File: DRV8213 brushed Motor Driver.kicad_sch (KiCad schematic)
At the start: 26 parts, among them J1 Keystone 3569, J10 1.27mm pin header, J11 1.27mm pin header, J2 Keystone 3579, J3 Keystone 3579, J4 Keystone 3569, J5 Keystone 3569, J6 Keystone 3579, J7 Keystone 3579, J8 Keystone 3569, J9 JST PH 2mm horizontal, U1 DRV8213RTER, U2 LP2981-3.3

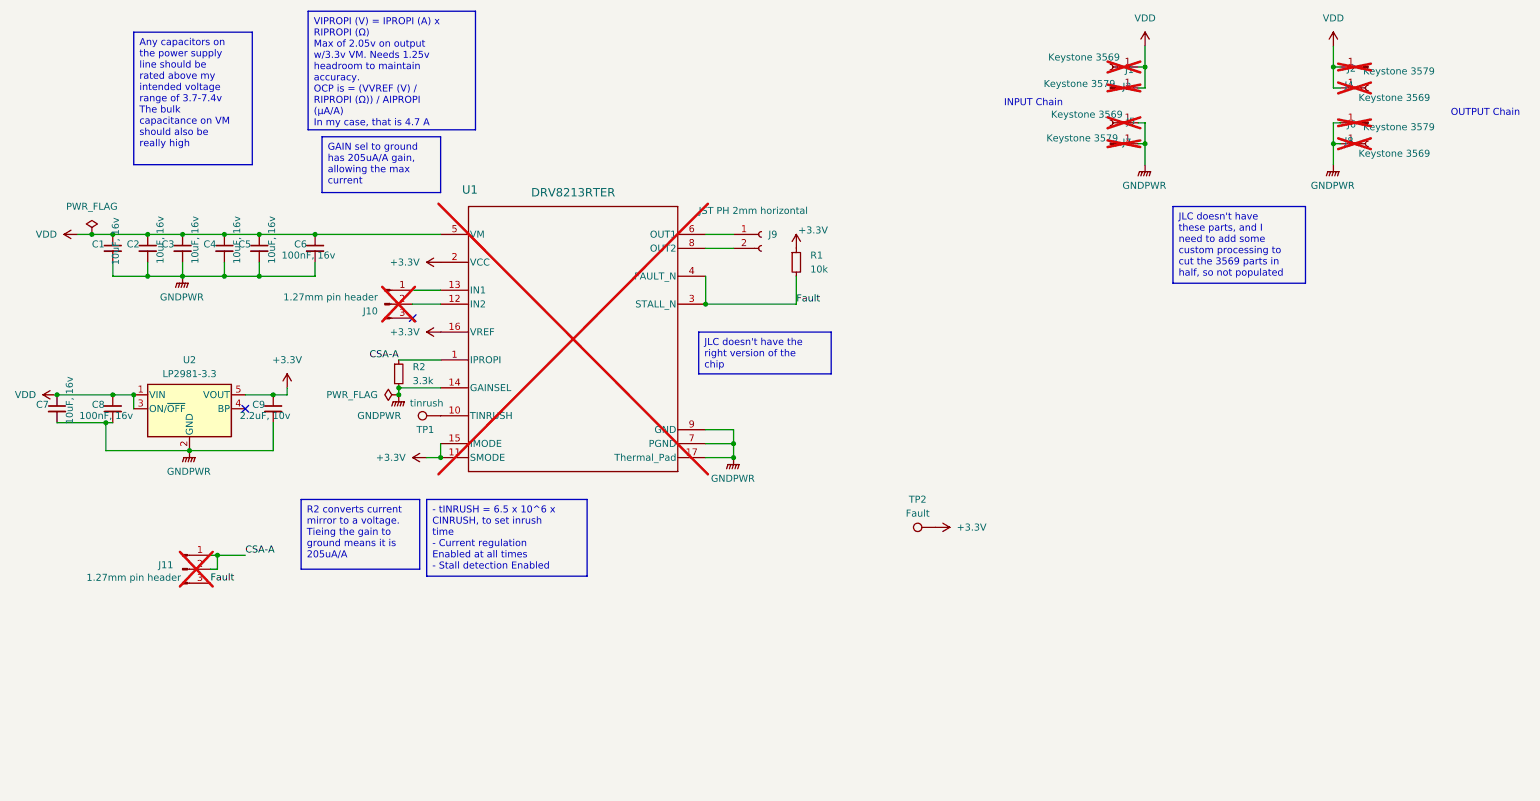
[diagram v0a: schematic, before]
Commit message: Updated connector parts in schematic
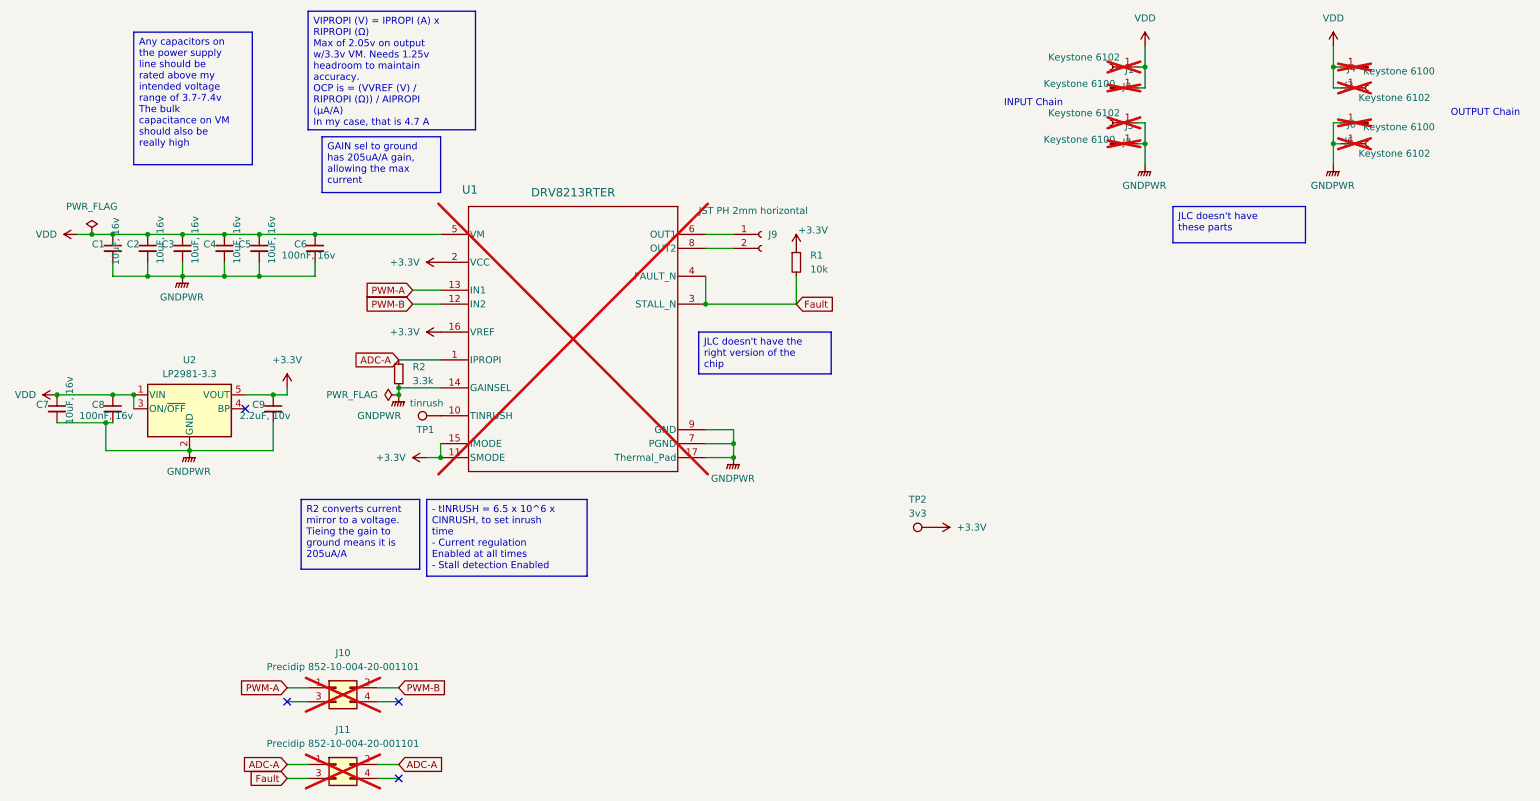
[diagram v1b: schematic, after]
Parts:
- removed J10, J11: 1.27mm pin header, Connector_PinHeader_1.27mm:PinHeader_1x03_P1.27mm_Horizontal, symbol Connector:Conn_01x03_Pin
- removed J2, J6: Keystone 3579, custom_Connector:Keystone_3579, symbol Connector:Conn_01x01_Pin
- removed J4, J8: Keystone 3569, custom_Connector:Keystone_3569_half, symbol Connector:Conn_01x01_Socket
- added J10, J11: Precidip 852-10-004-20-001101, custom_Connector:Precidip 852-10-004-20-001101, symbol Connector_Generic:Conn_02x02_Odd_Even
- added J2, J6: Keystone 6102, custom_Connector:Keystone_6102, symbol Connector:Conn_01x01_Socket
- added J4, J8: Keystone 6100, custom_Connector:Keystone_6100, symbol Connector:Conn_01x01_Pin
- J1, J5: value Keystone 3569 -> Keystone 6102; footprint custom_Connector:Keystone_3569_half -> custom_Connector:Keystone_6102
- J3, J7: value Keystone 3579 -> Keystone 6100; footprint custom_Connector:Keystone_3579 -> custom_Connector:Keystone_6100
- TP2: value Fault -> 3v3
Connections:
- net Fault: now also J11.3 (Pin_3)
- net GNDPWR: now also J6.1 (Pin_1), J8.1 (Pin_1)
- net VDD: now also J2.1 (Pin_1), J4.1 (Pin_1)
- net PWM-B: now reaches U1.12 (IN2)
- net PWM-B: now also J10.2 (Pin_2)
- net PWM-A: now reaches U1.13 (IN1)
- net PWM-A: now also J10.1 (Pin_1)
- net CSA-A renamed ADC-A
- net ADC-A: now also J11.1 (Pin_1), J11.2 (Pin_2)
- no-connect marks 2 -> 4
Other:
- title: (none) -> CACKLE - DRV8213 Driver
